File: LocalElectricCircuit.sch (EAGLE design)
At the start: 42 parts, among them IC1 PIC32MX360F512L, J1 Prog. Port, J3 Prog. Port, U1 ADS1118, U2 ADS1118

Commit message: ⏚⏚⏚
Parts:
- removed J3: Prog. Port, con-amp:520258-3
- added JP1: (no value), pinhead:PINHD-1X6
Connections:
- net GND_3V3: now also JP1.3; no longer J3.3
- net PIC16_3V3: now also JP1.2; no longer J3.2
- net PIC16_MCLR: now also JP1.1; no longer J3.1
- net PIC16_PGC: now also JP1.5; no longer J3.5
- net PIC16_PGD: now also JP1.4; no longer J3.4
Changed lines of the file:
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@@
 <part name="C10" library="resistor" deviceset="C-US" device="C1206" value="0.1uF"/>
 <part name="C11" library="resistor" deviceset="C-US" device="C1206" value="0.01uF"/>
-<part name="J3" library="con-amp" deviceset="520258-3" device="" value="Prog. Port"/>
 <part name="R7" library="rcl" deviceset="R-US_" device="M1206" value="50k"/>
 <part name="C12" library="resistor" deviceset="C-US" device="C1206" value="0.01uF"/>
@@
 <part name="PIC16_POWER_EN" library="pinhead" deviceset="PINHD-1X2" device=""/>
 <part name="R15" library="rcl" deviceset="R-US_" device="0309/12" value="1k"/>
+<part name="JP1" library="pinhead" deviceset="PINHD-1X6" device=""/>
 </parts>
 <sheets>
@@
 <instance part="C10" gate="G$1" x="231.14" y="25.4" rot="R90"/>
 <instance part="C11" gate="G$1" x="231.14" y="33.02" rot="R90"/>
-<instance part="J3" gate="G$1" x="292.1" y="5.08"/>
 <instance part="R7" gate="G$1" x="281.94" y="12.7" rot="R90"/>
 <instance part="C12" gate="G$1" x="-20.32" y="210.82"/>
@@
 <instance part="PIC16_POWER_EN" gate="G$1" x="289.56" y="30.48"/>
 <instance part="R15" gate="G$1" x="231.14" y="-73.66" rot="R180"/>
+<instance part="JP1" gate="A" x="292.1" y="2.54"/>
 </instances>
 <busses>
@@
 </segment>
 <segment>
-<pinref part="J3" gate="G$1" pin="3"/>
 <wire x1="289.56" y1="5.08" x2="279.4" y2="5.08" width="0.1524" layer="91"/>
 <label x="279.4" y="5.715" size="1.778" layer="95" rot="R180"/>
+<pinref part="JP1" gate="A" pin="3"/>
 </segment>
 <segment>
@@
 <junction x="281.94" y="17.78"/>
 <label x="279.4" y="18.415" size="1.778" layer="95" rot="R180"/>
-<pinref part="J3" gate="G$1" pin="1"/>
 <wire x1="289.56" y1="10.16" x2="287.02" y2="10.16" width="0.1524" layer="91"/>
 <wire x1="287.02" y1="17.78" x2="287.02" y2="10.16" width="0.1524" layer="91"/>
 <wire x1="279.4" y1="17.78" x2="281.94" y2="17.78" width="0.1524" layer="91"/>
+<pinref part="JP1" gate="A" pin="1"/>
 </segment>
 </net>
@@
 </segment>
 <segment>
-<pinref part="J3" gate="G$1" pin="4"/>
 <wire x1="289.56" y1="2.54" x2="279.4" y2="2.54" width="0.1524" layer="91"/>
 <label x="279.4" y="3.175" size="1.778" layer="95" rot="R180"/>
+<pinref part="JP1" gate="A" pin="4"/>
 </segment>
 </net>
@@
 </segment>
 <segment>
-<pinref part="J3" gate="G$1" pin="5"/>
 <wire x1="289.56" y1="0" x2="279.4" y2="0" width="0.1524" layer="91"/>
 <label x="279.4" y="0.635" size="1.778" layer="95" rot="R180"/>
+<pinref part="JP1" gate="A" pin="5"/>
 </segment>
 </net>
@@
 </segment>
 <segment>
-<pinref part="J3" gate="G$1" pin="2"/>
 <wire x1="289.56" y1="7.62" x2="281.94" y2="7.62" width="0.1524" layer="91"/>
 <pinref part="R7" gate="G$1" pin="1"/>
@@
 <label x="279.4" y="8.255" size="1.778" layer="95" rot="R180"/>
 <wire x1="279.4" y1="7.62" x2="281.94" y2="7.62" width="0.1524" layer="91"/>
-</segment>
-<segment>
+<pinref part="JP1" gate="A" pin="2"/>
+</segment>
+<segment>

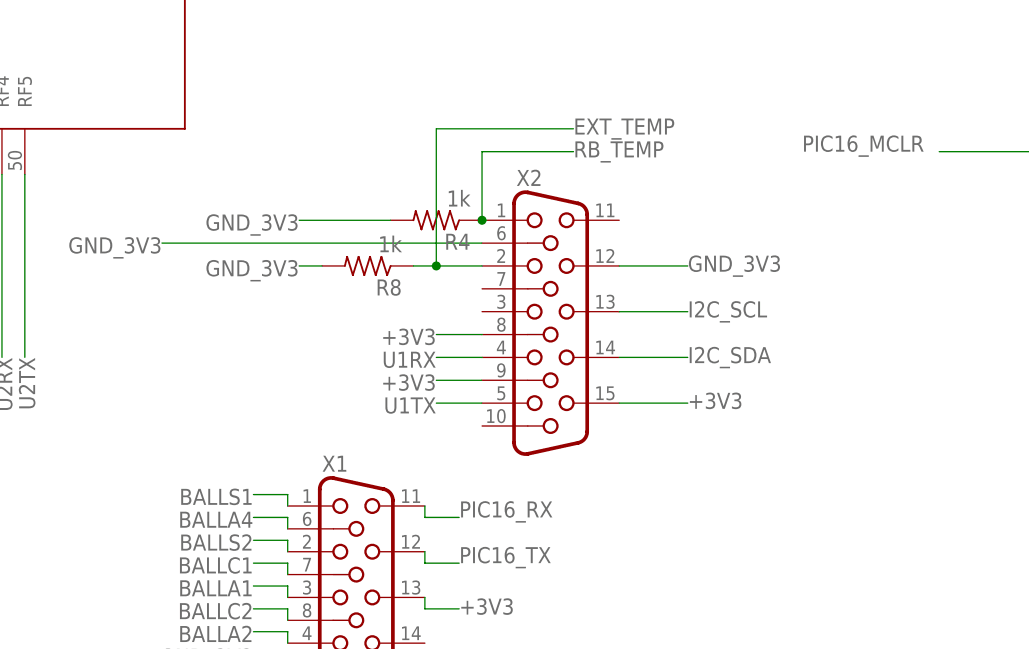
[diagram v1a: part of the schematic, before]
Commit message: Added Male VGA part
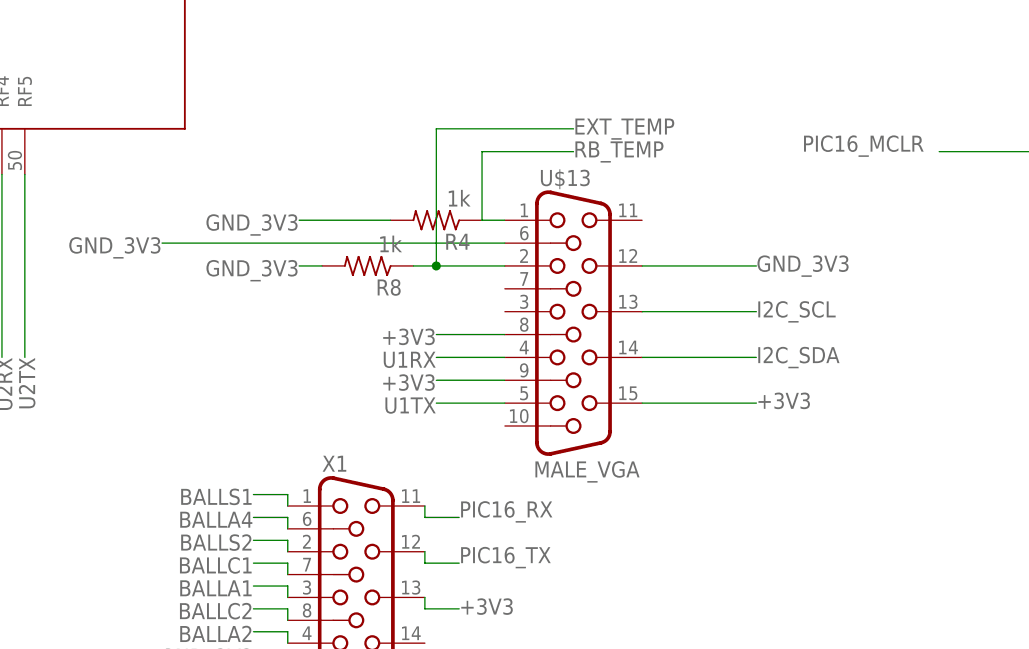
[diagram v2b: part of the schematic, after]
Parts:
- removed X2: (no value), con-subd:HF15H
- added U$13: MALE_VGA, MALE_VGA:MALE_VGA
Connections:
- net +3V3: now also U$13.15, U$13.8, U$13.9; no longer X2.15, X2.8, X2.9
- net EXT_TEMP: now also U$13.2; no longer X2.2
- net GND_3V3: now also U$13.12, U$13.6; no longer X2.12, X2.6
- net I2C_SCL: now also U$13.13; no longer X2.13
- net I2C_SDA: now also U$13.14; no longer X2.14
- net RB_TEMP: now also U$13.1; no longer X2.1
- net U1RX: now also U$13.4; no longer X2.4
- net U1TX: now also U$13.5; no longer X2.5
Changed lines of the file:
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@@
 <part name="J2" library="19inch_VG96KB" deviceset="VG96" device="KB"/>
 <part name="X1" library="con-subd" deviceset="HF15" device="H"/>
-<part name="X2" library="con-subd" deviceset="HF15" device="H"/>
 <part name="C8" library="resistor" deviceset="C-US" device="C1206" value="0.1uF"/>
 <part name="C9" library="resistor" deviceset="C-US" device="C1206" value="0.1uF"/>
@@
 <part name="R15" library="rcl" deviceset="R-US_" device="0309/12" value="1k"/>
 <part name="JP1" library="pinhead" deviceset="PINHD-1X6" device=""/>
+<part name="U$13" library="MALE_VGA" deviceset="MALE_VGA" device=""/>
 </parts>
 <sheets>
@@
 <instance part="J2" gate="G$1" x="-35.56" y="66.04" rot="MR0"/>
 <instance part="X1" gate="G$1" x="138.43" y="-39.37"/>
-<instance part="X2" gate="G$1" x="160.02" y="-7.62"/>
 <instance part="C8" gate="G$1" x="193.04" y="76.2"/>
 <instance part="C9" gate="G$1" x="193.04" y="114.3"/>
@@
 <instance part="R15" gate="G$1" x="231.14" y="-73.66" rot="R180"/>
 <instance part="JP1" gate="A" x="292.1" y="2.54"/>
+<instance part="U$13" gate="G$1" x="162.56" y="-7.62"/>
 </instances>
 <busses>
@@
 </segment>
 <segment>
-<pinref part="X2" gate="G$1" pin="15"/>
-<wire x1="167.64" y1="-17.78" x2="175.26" y2="-17.78" width="0.1524" layer="91"/>
-<label x="175.26" y="-18.415" size="1.778" layer="95"/>
-</segment>
-<segment>
-<pinref part="X2" gate="G$1" pin="8"/>
-<wire x1="152.4" y1="-10.16" x2="147.32" y2="-10.16" width="0.1524" layer="91"/>
+<wire x1="170.18" y1="-17.78" x2="182.88" y2="-17.78" width="0.1524" layer="91"/>
+<label x="182.88" y="-18.415" size="1.778" layer="95"/>
+<pinref part="U$13" gate="G$1" pin="15"/>
+</segment>
+<segment>
+<wire x1="154.94" y1="-10.16" x2="147.32" y2="-10.16" width="0.1524" layer="91"/>
 <label x="147.32" y="-9.525" size="1.778" layer="95" rot="R180"/>
-</segment>
-<segment>
-<pinref part="X2" gate="G$1" pin="9"/>
-<wire x1="152.4" y1="-15.24" x2="147.32" y2="-15.24" width="0.1524" layer="91"/>
+<pinref part="U$13" gate="G$1" pin="8"/>
+</segment>
+<segment>
+<wire x1="154.94" y1="-15.24" x2="147.32" y2="-15.24" width="0.1524" layer="91"/>
 <label x="147.32" y="-14.605" size="1.778" layer="95" rot="R180"/>
+<pinref part="U$13" gate="G$1" pin="9"/>
 </segment>
 <segment>
@@
 </segment>
 <segment>
-<pinref part="X2" gate="G$1" pin="12"/>
-<wire x1="167.64" y1="-2.54" x2="175.26" y2="-2.54" width="0.1524" layer="91"/>
-<label x="175.26" y="-3.175" size="1.778" layer="95"/>
+<wire x1="170.18" y1="-2.54" x2="182.88" y2="-2.54" width="0.1524" layer="91"/>
+<label x="182.88" y="-3.175" size="1.778" layer="95"/>
+<pinref part="U$13" gate="G$1" pin="12"/>
 </segment>
 <segment>
@@
 </segment>
 <segment>
-<pinref part="X2" gate="G$1" pin="6"/>
-<wire x1="152.4" y1="0" x2="116.84" y2="0" width="0.1524" layer="91"/>
+<wire x1="154.94" y1="0" x2="116.84" y2="0" width="0.1524" layer="91"/>
 <label x="116.84" y="0.635" size="1.778" layer="95" rot="R180"/>
+<pinref part="U$13" gate="G$1" pin="6"/>
 </segment>
 </net>
@@
 </segment>
 <segment>
-<pinref part="X2" gate="G$1" pin="4"/>
-<wire x1="152.4" y1="-12.7" x2="147.32" y2="-12.7" width="0.1524" layer="91"/>
+<wire x1="154.94" y1="-12.7" x2="147.32" y2="-12.7" width="0.1524" layer="91"/>
 <label x="147.32" y="-12.065" size="1.778" layer="95" rot="R180"/>
+<pinref part="U$13" gate="G$1" pin="4"/>
 </segment>
 </net>
@@
 </segment>
 <segment>
-<pinref part="X2" gate="G$1" pin="5"/>
-<wire x1="152.4" y1="-17.78" x2="147.32" y2="-17.78" width="0.1524" layer="91"/>
+<wire x1="154.94" y1="-17.78" x2="147.32" y2="-17.78" width="0.1524" layer="91"/>
 <label x="147.32" y="-17.145" size="1.778" layer="95" rot="R180"/>
+<pinref part="U$13" gate="G$1" pin="5"/>
 </segment>
 </net>
@@
 <wire x1="147.32" y1="-2.54" x2="147.32" y2="12.7" width="0.1524" layer="91"/>
 <wire x1="147.32" y1="12.7" x2="162.56" y2="12.7" width="0.1524" layer="91"/>
-<pinref part="X2" gate="G$1" pin="2"/>
-<wire x1="152.4" y1="-2.54" x2="147.32" y2="-2.54" width="0.1524" layer="91"/>
+<wire x1="154.94" y1="-2.54" x2="147.32" y2="-2.54" width="0.1524" layer="91"/>
 <junction x="147.32" y="-2.54"/>
+<pinref part="U$13" gate="G$1" pin="2"/>
 </segment>
 </net>
@@
 <segment>
 <label x="162.56" y="9.525" size="1.778" layer="95"/>
-<pinref part="X2" gate="G$1" pin="1"/>
 <pinref part="R4" gate="G$1" pin="1"/>
-<junction x="152.4" y="2.54"/>
 <wire x1="152.4" y1="2.54" x2="152.4" y2="10.16" width="0.1524" layer="91"/>
 <wire x1="152.4" y1="10.16" x2="162.56" y2="10.16" width="0.1524" layer="91"/>
+<pinref part="U$13" gate="G$1" pin="1"/>
+<wire x1="152.4" y1="2.54" x2="154.94" y2="2.54" width="0.1524" layer="91"/>
 </segment>
 </net>
@@
 <net name="I2C_SCL" class="0">
 <segment>
-<label x="175.26" y="-8.255" size="1.778" layer="95"/>
-<wire x1="175.26" y1="-7.62" x2="167.64" y2="-7.62" width="0.1524" layer="91"/>
-<pinref part="X2" gate="G$1" pin="13"/>
+<label x="182.88" y="-8.255" size="1.778" layer="95"/>
+<wire x1="182.88" y1="-7.62" x2="170.18" y2="-7.62" width="0.1524" layer="91"/>
+<pinref part="U$13" gate="G$1" pin="13"/>
 </segment>
 <segment>
@@
 <net name="I2C_SDA" class="0">
 <segment>
-<label x="175.26" y="-13.335" size="1.778" layer="95"/>
-<wire x1="167.64" y1="-12.7" x2="175.26" y2="-12.7" width="0.1524" layer="91"/>
-<pinref part="X2" gate="G$1" pin="14"/>
-</segment>
-<segment>
+<label x="182.88" y="-13.335" size="1.778" layer="95"/>
+<wire x1="170.18" y1="-12.7" x2="182.88" y2="-12.7" width="0.1524" layer="91"/>
+<pinref part="U$13" gate="G$1" pin="14"/>
+</segment>
+<segment>

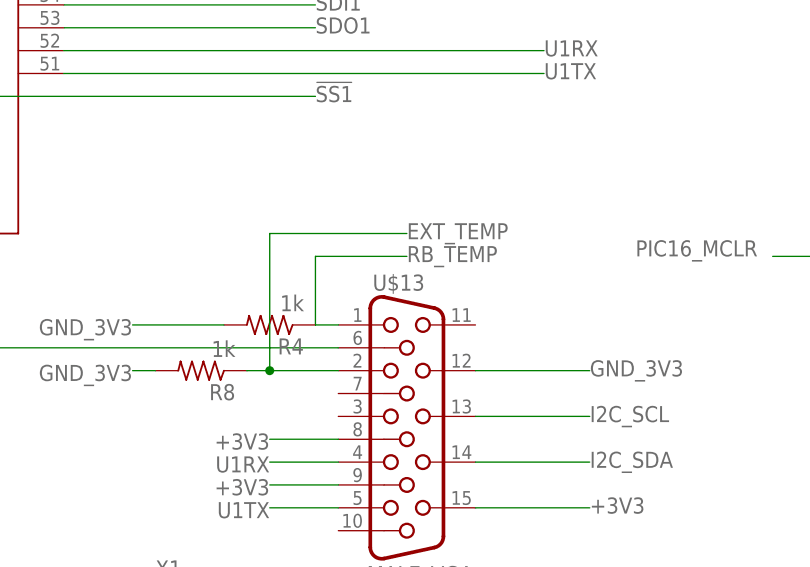
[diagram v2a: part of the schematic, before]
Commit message: male VGA connector has been auto-routed
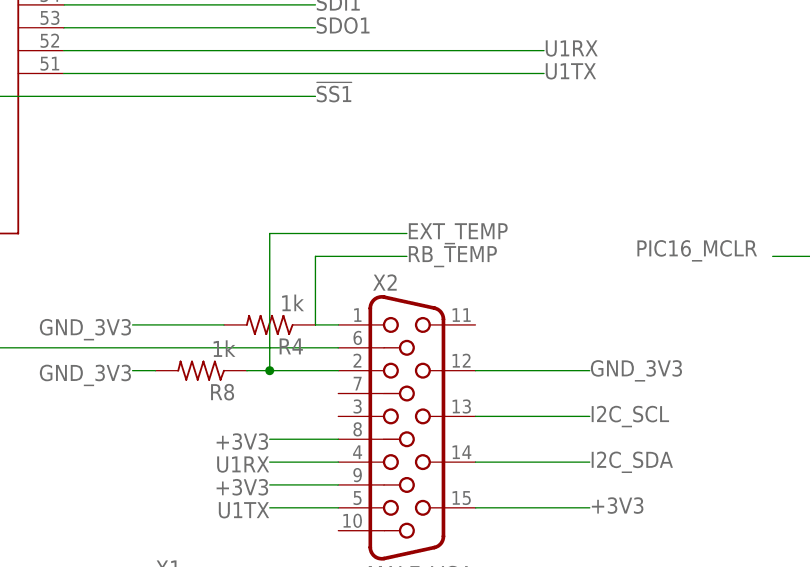
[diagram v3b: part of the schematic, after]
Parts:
- renumbered U$13 to X2
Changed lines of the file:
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@@
 <part name="R15" library="rcl" deviceset="R-US_" device="0309/12" value="1k"/>
 <part name="JP1" library="pinhead" deviceset="PINHD-1X6" device=""/>
-<part name="U$13" library="MALE_VGA" deviceset="MALE_VGA" device=""/>
+<part name="X2" library="MALE_VGA" deviceset="MALE_VGA" device=""/>
 </parts>
 <sheets>
@@
 <instance part="R15" gate="G$1" x="231.14" y="-73.66" rot="R180"/>
 <instance part="JP1" gate="A" x="292.1" y="2.54"/>
-<instance part="U$13" gate="G$1" x="162.56" y="-7.62"/>
+<instance part="X2" gate="G$1" x="162.56" y="-7.62"/>
 </instances>
 <busses>
@@
 <wire x1="170.18" y1="-17.78" x2="182.88" y2="-17.78" width="0.1524" layer="91"/>
 <label x="182.88" y="-18.415" size="1.778" layer="95"/>
-<pinref part="U$13" gate="G$1" pin="15"/>
+<pinref part="X2" gate="G$1" pin="15"/>
 </segment>
 <segment>
 <wire x1="154.94" y1="-10.16" x2="147.32" y2="-10.16" width="0.1524" layer="91"/>
 <label x="147.32" y="-9.525" size="1.778" layer="95" rot="R180"/>
-<pinref part="U$13" gate="G$1" pin="8"/>
+<pinref part="X2" gate="G$1" pin="8"/>
 </segment>
 <segment>
 <wire x1="154.94" y1="-15.24" x2="147.32" y2="-15.24" width="0.1524" layer="91"/>
 <label x="147.32" y="-14.605" size="1.778" layer="95" rot="R180"/>
-<pinref part="U$13" gate="G$1" pin="9"/>
+<pinref part="X2" gate="G$1" pin="9"/>
 </segment>
 <segment>
@@
 <wire x1="170.18" y1="-2.54" x2="182.88" y2="-2.54" width="0.1524" layer="91"/>
 <label x="182.88" y="-3.175" size="1.778" layer="95"/>
-<pinref part="U$13" gate="G$1" pin="12"/>
+<pinref part="X2" gate="G$1" pin="12"/>
 </segment>
 <segment>
@@
 <wire x1="154.94" y1="0" x2="116.84" y2="0" width="0.1524" layer="91"/>
 <label x="116.84" y="0.635" size="1.778" layer="95" rot="R180"/>
-<pinref part="U$13" gate="G$1" pin="6"/>
+<pinref part="X2" gate="G$1" pin="6"/>
 </segment>
 </net>
@@
 <wire x1="154.94" y1="-12.7" x2="147.32" y2="-12.7" width="0.1524" layer="91"/>
 <label x="147.32" y="-12.065" size="1.778" layer="95" rot="R180"/>
-<pinref part="U$13" gate="G$1" pin="4"/>
+<pinref part="X2" gate="G$1" pin="4"/>
 </segment>
 </net>
@@
 <wire x1="154.94" y1="-17.78" x2="147.32" y2="-17.78" width="0.1524" layer="91"/>
 <label x="147.32" y="-17.145" size="1.778" layer="95" rot="R180"/>
-<pinref part="U$13" gate="G$1" pin="5"/>
+<pinref part="X2" gate="G$1" pin="5"/>
 </segment>
 </net>
@@
 <wire x1="154.94" y1="-2.54" x2="147.32" y2="-2.54" width="0.1524" layer="91"/>
 <junction x="147.32" y="-2.54"/>
-<pinref part="U$13" gate="G$1" pin="2"/>
+<pinref part="X2" gate="G$1" pin="2"/>
 </segment>
 </net>
@@
 <wire x1="152.4" y1="2.54" x2="152.4" y2="10.16" width="0.1524" layer="91"/>
 <wire x1="152.4" y1="10.16" x2="162.56" y2="10.16" width="0.1524" layer="91"/>
-<pinref part="U$13" gate="G$1" pin="1"/>
+<pinref part="X2" gate="G$1" pin="1"/>
 <wire x1="152.4" y1="2.54" x2="154.94" y2="2.54" width="0.1524" layer="91"/>
 </segment>
@@
 <label x="182.88" y="-8.255" size="1.778" layer="95"/>
 <wire x1="182.88" y1="-7.62" x2="170.18" y2="-7.62" width="0.1524" layer="91"/>
-<pinref part="U$13" gate="G$1" pin="13"/>
+<pinref part="X2" gate="G$1" pin="13"/>
 </segment>
 <segment>
@@
 <label x="182.88" y="-13.335" size="1.778" layer="95"/>
 <wire x1="170.18" y1="-12.7" x2="182.88" y2="-12.7" width="0.1524" layer="91"/>
-<pinref part="U$13" gate="G$1" pin="14"/>
-</segment>
-<segment>
+<pinref part="X2" gate="G$1" pin="14"/>
+</segment>
+<segment>
